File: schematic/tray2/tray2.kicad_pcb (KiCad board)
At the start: 2 copper layers, 52.1 x 100.3 mm, 57 parts, among them J1 AVR-ISP-10, J2 Conn_02x10_Odd_Even, J3 Conn_Coaxial, J4 Conn_Coaxial, J5 Conn_Coaxial, Q1 BF998, Q2 BFP196, Q3 BC847, Q4 BC847, U1 74AC253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

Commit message: Update pcb to fix issue
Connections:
- U4 pad 7: Net-(J2-Pad5) -> Net-(J2-Pad15)
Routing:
- net Net-(J2-Pad5): track 31.8 -> 0.00 mm, vias 2 -> 0
- net Net-(J2-Pad15): track 0.00 -> 26.4 mm, vias 0 -> 2
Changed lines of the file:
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@@
-(kicad_pcb (version 20171130) (host pcbnew 5.1.4)
+(kicad_pcb (version 20171130) (host pcbnew 5.1.5)
   (general
     (thickness 1.6)
     (drawings 6)
-    (tracks 391)
+    (tracks 388)
     (zones 0)
     (modules 57)
@@
       (net 74 "Net-(U4-Pad8)"))
     (pad 7 smd rect (at -4.25 -2 270) (size 1.6 0.55) (layers B.Cu B.Paste B.Mask)
-      (net 38 "Net-(J2-Pad5)"))
+      (net 33 "Net-(J2-Pad15)"))
     (pad 6 smd rect (at -4.25 -1.2 270) (size 1.6 0.55) (layers B.Cu B.Paste B.Mask)
       (net 29 VCC))
@@
   (segment (start 32.639 160.909) (end 30.48 158.75) (width 0.25) (layer B.Cu) (net 32))
   (segment (start 32.639 164.338) (end 32.639 160.909) (width 0.25) (layer B.Cu) (net 32))
-  (segment (start 31.701314 173.99) (end 31.955314 174.244) (width 0.25) (layer B.Cu) (net 38))
-  (segment (start 30.48 173.99) (end 31.701314 173.99) (width 0.25) (layer B.Cu) (net 38))
-  (segment (start 31.955314 174.244) (end 33.782 174.244) (width 0.25) (layer B.Cu) (net 38))
-  (via (at 33.782 174.244) (size 0.8) (drill 0.4) (layers F.Cu B.Cu) (net 38))
-  (segment (start 33.782 174.244) (end 41.148 174.244) (width 0.25) (layer F.Cu) (net 38))
-  (segment (start 41.148 174.244) (end 54.102 161.29) (width 0.25) (layer F.Cu) (net 38))
-  (via (at 54.102 161.29) (size 0.8) (drill 0.4) (layers F.Cu B.Cu) (net 38))
-  (segment (start 54.102 163.993) (end 54.07 164.025) (width 0.25) (layer B.Cu) (net 38))
-  (segment (start 54.102 161.29) (end 54.102 163.993) (width 0.25) (layer B.Cu) (net 38))
+  (via (at 54.102 161.29) (size 0.8) (drill 0.4) (layers F.Cu B.Cu) (net 33))
+  (segment (start 54.102 163.993) (end 54.07 164.025) (width 0.25) (layer B.Cu) (net 33))
+  (segment (start 54.102 161.29) (end 54.102 163.993) (width 0.25) (layer B.Cu) (net 33))
+  (segment (start 30.48 161.29) (end 31.89 161.29) (width 0.25) (layer B.Cu) (net 33))
+  (via (at 31.89 161.29) (size 0.8) (drill 0.4) (layers F.Cu B.Cu) (net 33))
+  (segment (start 31.89 161.29) (end 54.102 161.29) (width 0.25) (layer F.Cu) (net 33))
   (segment (start 39.37 138.43) (end 39.497 138.557) (width 0.25) (layer B.Cu) (net 40))
   (segment (start 36.83 138.43) (end 39.37 138.43) (width 0.25) (layer B.Cu) (net 40))

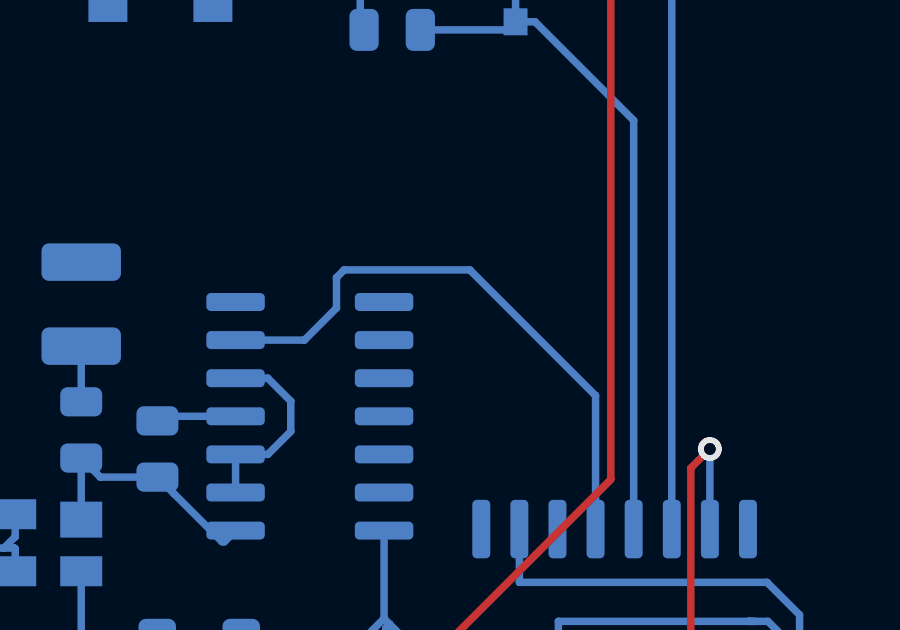
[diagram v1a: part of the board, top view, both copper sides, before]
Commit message: Add gnd to oe pin
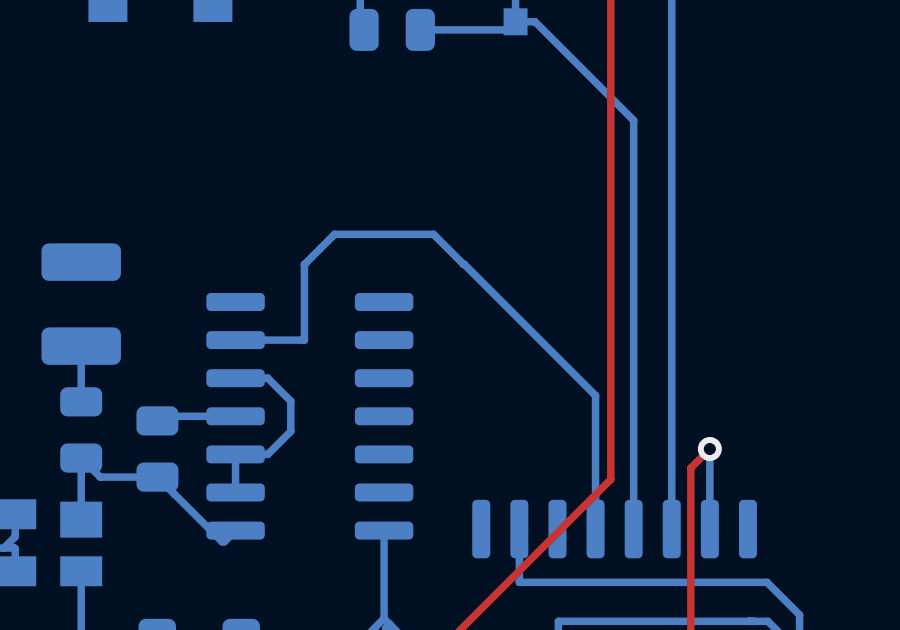
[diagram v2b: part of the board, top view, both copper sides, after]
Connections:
- U1 pad 1: Net-(U1-Pad1) -> GND
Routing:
- net Net-(U1-Pad4): track 19.7 -> 21.6 mm

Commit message: Change transistor with bigger fT
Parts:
- Q3, Q4: value BC847 -> BFR92A
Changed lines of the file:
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@@
       (effects (font (size 1 1) (thickness 0.15)) (justify mirror))
     )
-    (fp_text value BC847 (at 0 -2.5 90) (layer B.Fab)
+    (fp_text value BFR92A (at 0 -2.5 90) (layer B.Fab)
       (effects (font (size 1 1) (thickness 0.15)) (justify mirror))
     )
@@
       (effects (font (size 1 1) (thickness 0.15)) (justify mirror))
     )
-    (fp_text value BC847 (at 0 -2.5 90) (layer B.Fab)
+    (fp_text value BFR92A (at 0 -2.5 90) (layer B.Fab)
       (effects (font (size 1 1) (thickness 0.15)) (justify mirror))
     )

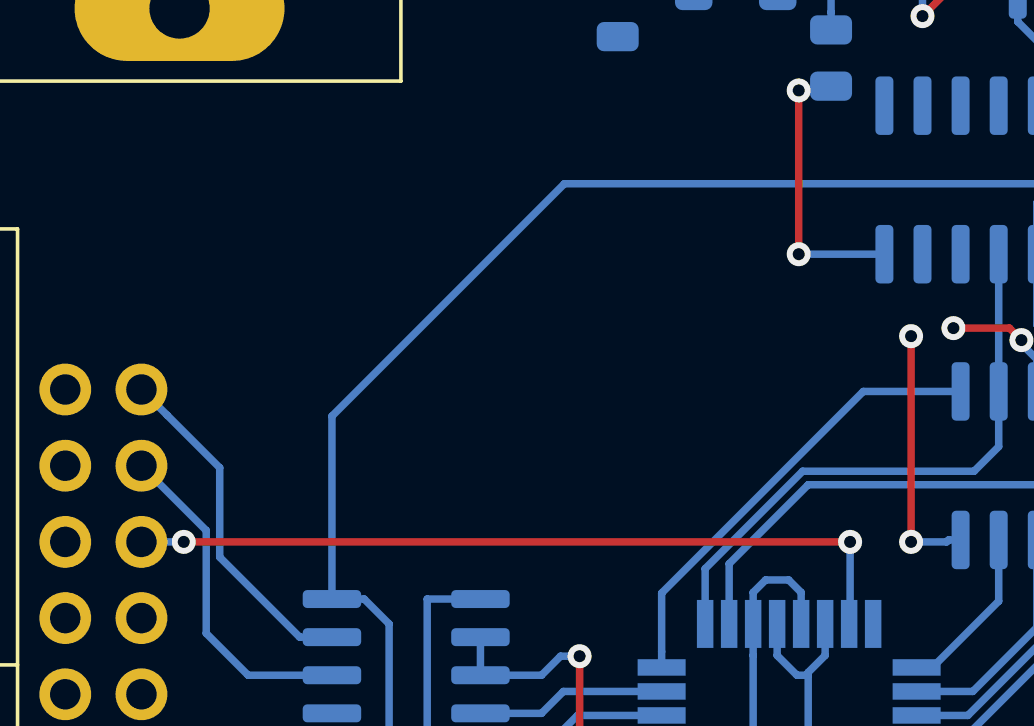
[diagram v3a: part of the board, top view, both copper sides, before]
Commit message: Add capacitor on path of clock
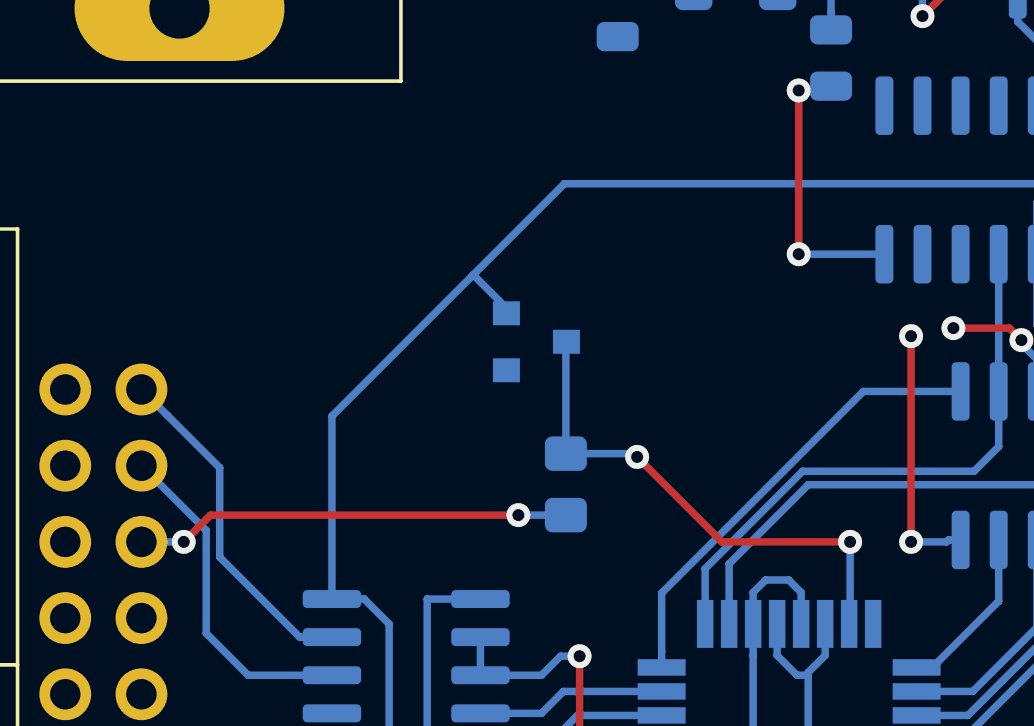
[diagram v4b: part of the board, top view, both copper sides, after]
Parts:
- added C14: 100n, Capacitor_SMD:C_0805_2012Metric_Pad1.15x1.40mm_HandSolder, B.Cu at (44.6, 159.4)
- added D4: BAT54S, Package_TO_SOT_SMD:SOT-23, B.Cu at (43.6, 154.6)
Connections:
- J2 pad 15: Net-(J2-Pad15) -> Net-(C14-Pad1)
- U4 pad 7: Net-(J2-Pad15) -> Net-(C14-Pad2)
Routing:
- net Net-(J2-Pad15): track 26.4 -> 0.00 mm, vias 2 -> 0
- net Net-(C14-Pad2): track 0.00 -> 17.2 mm, vias 0 -> 2
- net Net-(C14-Pad1): track 0.00 -> 14.5 mm, vias 0 -> 2
- net VCC: track 215.8 -> 217.6 mm

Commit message: Use 100 resistor instead capacitor
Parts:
- R18: renamed from C14; value 100n -> 100; footprint Capacitor_SMD:C_0805_2012Metric_Pad1.15x1.40mm_HandSolder -> Resistor_SMD:R_0805_2012Metric_Pad1.15x1.40mm_HandSolder

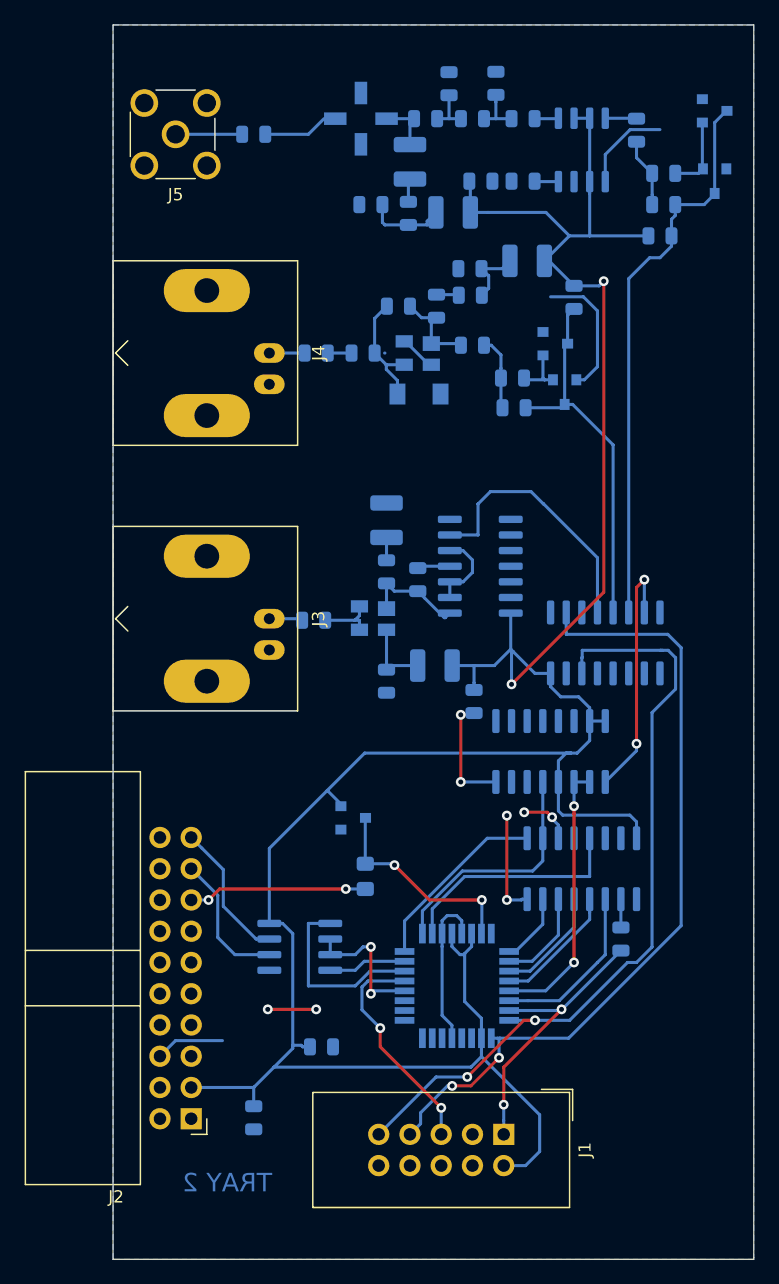
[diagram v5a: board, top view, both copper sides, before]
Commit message: Use tested MB506 prescaler
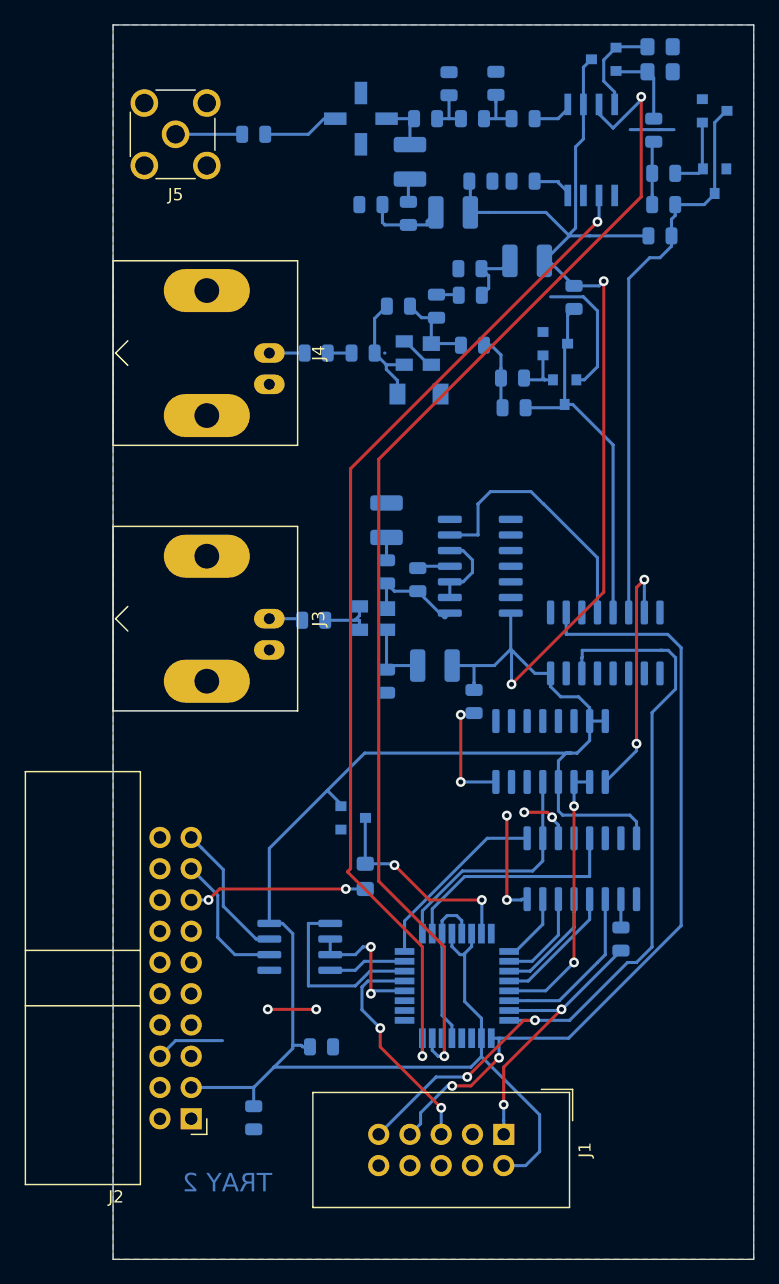
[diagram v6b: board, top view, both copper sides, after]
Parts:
- added Q5: BFR92A, Package_TO_SOT_SMD:SOT-23, B.Cu at (64.0, 93.0)
- added R19: 2k7, Resistor_SMD:R_0805_2012Metric_Pad1.15x1.40mm_HandSolder, B.Cu at (68.6, 91.9)
- added R20: 680, Resistor_SMD:R_0805_2012Metric_Pad1.15x1.40mm_HandSolder, B.Cu at (68.6, 94.0)
- R13: value 150 -> 50
- R14: value 39 -> 0
- R15: value 150 -> DNP
- R9: value 2k2 -> 8k2
- U9: value MC12032 -> MB506; footprint Package_SO:SO-8_3.9x4.9mm_P1.27mm -> Package_SO:SO-8_5.3x6.2mm_P1.27mm
- moved C5 1.40 mm to (68.1, 98.7)
- moved U9 0.76 mm to (63.0, 100.3)
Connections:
- U4 pad 23: Net-(U4-Pad23) -> PC0
- U4 pad 24: Net-(U4-Pad24) -> PC1
- U9 pad 3: VCC -> PC0
- U9 pad 4: Net-(C5-Pad2) -> Net-(Q5-Pad1)
- U9 pad 6: VCC -> PC1
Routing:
- net PC0: track 0.00 -> 97.1 mm, vias 0 -> 2
- net PC1: track 0.00 -> 82.4 mm, vias 0 -> 2
- net Net-(Q5-Pad1): track 0.00 -> 7.98 mm
- net VCC: track 217.6 -> 221.7 mm
- net Net-(C5-Pad2): track 2.55 -> 6.60 mm
- net GND: track 65.1 -> 61.3 mm
- net Net-(C10-Pad1): track 1.95 -> 3.44 mm
- net Net-(C9-Pad1): track 1.95 -> 3.39 mm

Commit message: In HF change resistor so it works better with CMOS inputs - now working up to 100MHz before 90MHz
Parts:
- R6: value 2k2 -> 8k2
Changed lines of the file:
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@@
       (effects (font (size 1 1) (thickness 0.15)) (justify mirror))
     )
-    (fp_text value 2k2 (at 0 -1.65) (layer B.Fab)
+    (fp_text value 8k2 (at 0 -1.65) (layer B.Fab)
       (effects (font (size 1 1) (thickness 0.15)) (justify mirror))
     )
@@
   (segment (start 32.639 160.909) (end 30.48 158.75) (width 0.25) (layer B.Cu) (net 32))
   (segment (start 32.639 164.338) (end 32.639 160.909) (width 0.25) (layer B.Cu) (net 32))
-  (via (at 54.102 161.29) (size 0.8) (drill 0.4) (layers F.Cu B.Cu) (net 83))
-  (segment (start 54.102 163.993) (end 54.07 164.025) (width 0.25) (layer B.Cu) (net 83))
-  (segment (start 54.102 161.29) (end 54.102 163.993) (width 0.25) (layer B.Cu) (net 83))
   (segment (start 30.48 161.29) (end 31.89 161.29) (width 0.25) (layer B.Cu) (net 33))
   (via (at 31.89 161.29) (size 0.8) (drill 0.4) (layers F.Cu B.Cu) (net 33))
+  (segment (start 44.6278 160.3973) (end 43.044 160.3973) (width 0.25) (layer B.Cu) (net 33))
+  (via (at 43.044 160.3973) (size 0.8) (drill 0.4) (layers F.Cu B.Cu) (net 33))
+  (segment (start 32.7827 160.3973) (end 31.89 161.29) (width 0.25) (layer F.Cu) (net 33))
+  (segment (start 43.044 160.3973) (end 32.7827 160.3973) (width 0.25) (layer F.Cu) (net 33))
   (segment (start 39.37 138.43) (end 39.497 138.557) (width 0.25) (layer B.Cu) (net 40))
   (segment (start 36.83 138.43) (end 39.37 138.43) (width 0.25) (layer B.Cu) (net 40))
@@
   (segment (start 51.5 134.165) (end 49.0475 134.165) (width 0.25) (layer B.Cu) (net 80))
   (segment (start 65.405 163.5275) (end 65.405 161.225) (width 0.25) (layer B.Cu) (net 82))
+  (via (at 54.102 161.29) (size 0.8) (drill 0.4) (layers F.Cu B.Cu) (net 83))
+  (segment (start 54.102 163.993) (end 54.07 164.025) (width 0.25) (layer B.Cu) (net 83))
+  (segment (start 54.102 161.29) (end 54.102 163.993) (width 0.25) (layer B.Cu) (net 83))
   (segment (start 44.6278 154.6388) (end 44.6466 154.62) (width 0.25) (layer B.Cu) (net 83))
   (segment (start 44.6278 158.3473) (end 44.6278 154.6388) (width 0.25) (layer B.Cu) (net 83))
@@
   (segment (start 46.8921 158.3473) (end 44.6278 158.3473) (width 0.25) (layer B.Cu) (net 83))
   (segment (start 47.0027 158.4579) (end 46.8921 158.3473) (width 0.25) (layer B.Cu) (net 83))
-  (segment (start 44.6278 160.3973) (end 43.044 160.3973) (width 0.25) (layer B.Cu) (net 33))
-  (via (at 43.044 160.3973) (size 0.8) (drill 0.4) (layers F.Cu B.Cu) (net 33))
-  (segment (start 32.7827 160.3973) (end 31.89 161.29) (width 0.25) (layer F.Cu) (net 33))
-  (segment (start 43.044 160.3973) (end 32.7827 160.3973) (width 0.25) (layer F.Cu) (net 33))
   (segment (start 65.074 91.948) (end 65.008 92.014) (width 0.25) (layer B.Cu) (net 84))
   (segment (start 67.564 91.948) (end 65.074 91.948) (width 0.25) (layer B.Cu) (net 84))
